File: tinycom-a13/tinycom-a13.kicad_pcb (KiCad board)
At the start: 4 copper layers, 39.4 x 41.1 mm, 23 parts, among them P1 CONN_02X08, P2 CONN_02X08, U1 IC_A13, U2 H5TQ2G83BFR/FBGA82, Y1 Crystal

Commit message: prepare base
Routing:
- net VCC_30: track 42.4 -> 45.3 mm
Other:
- rule pad_to_mask_clearance: 0.2 -> 0.07

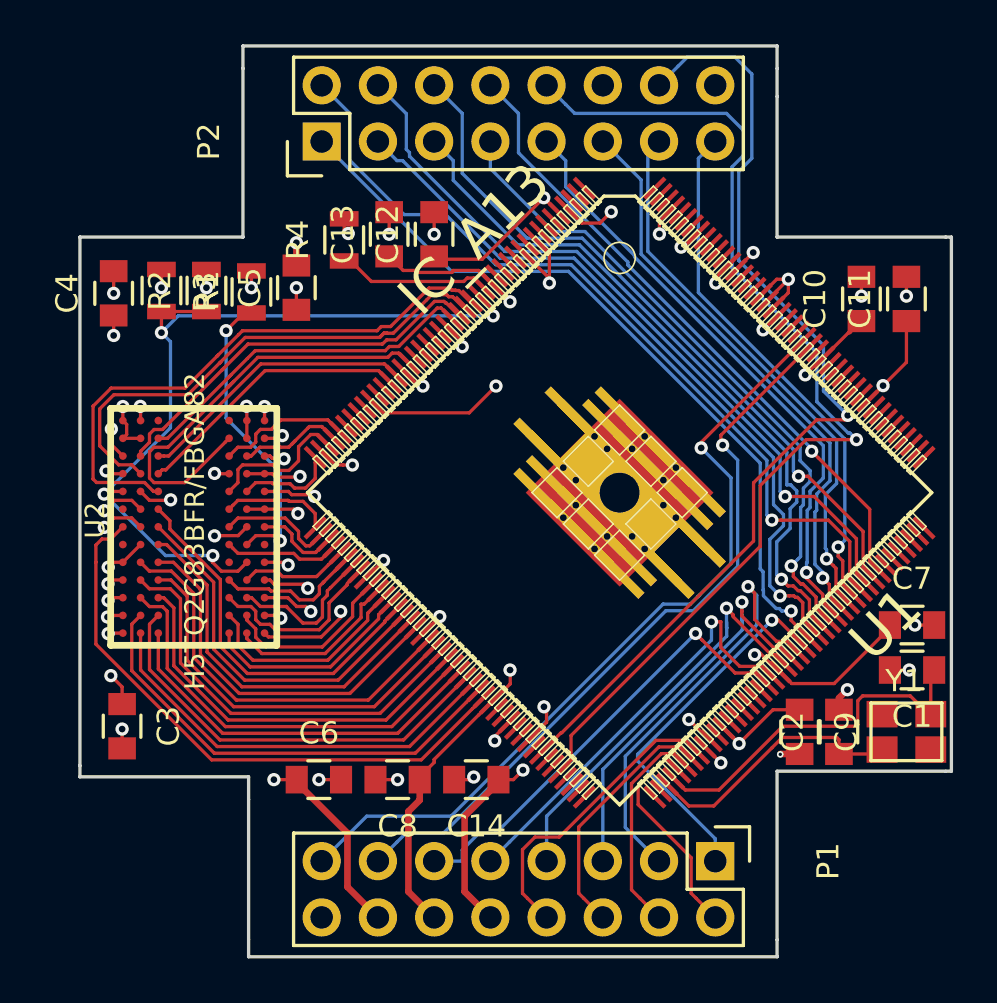
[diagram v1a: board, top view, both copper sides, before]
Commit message: change connectors
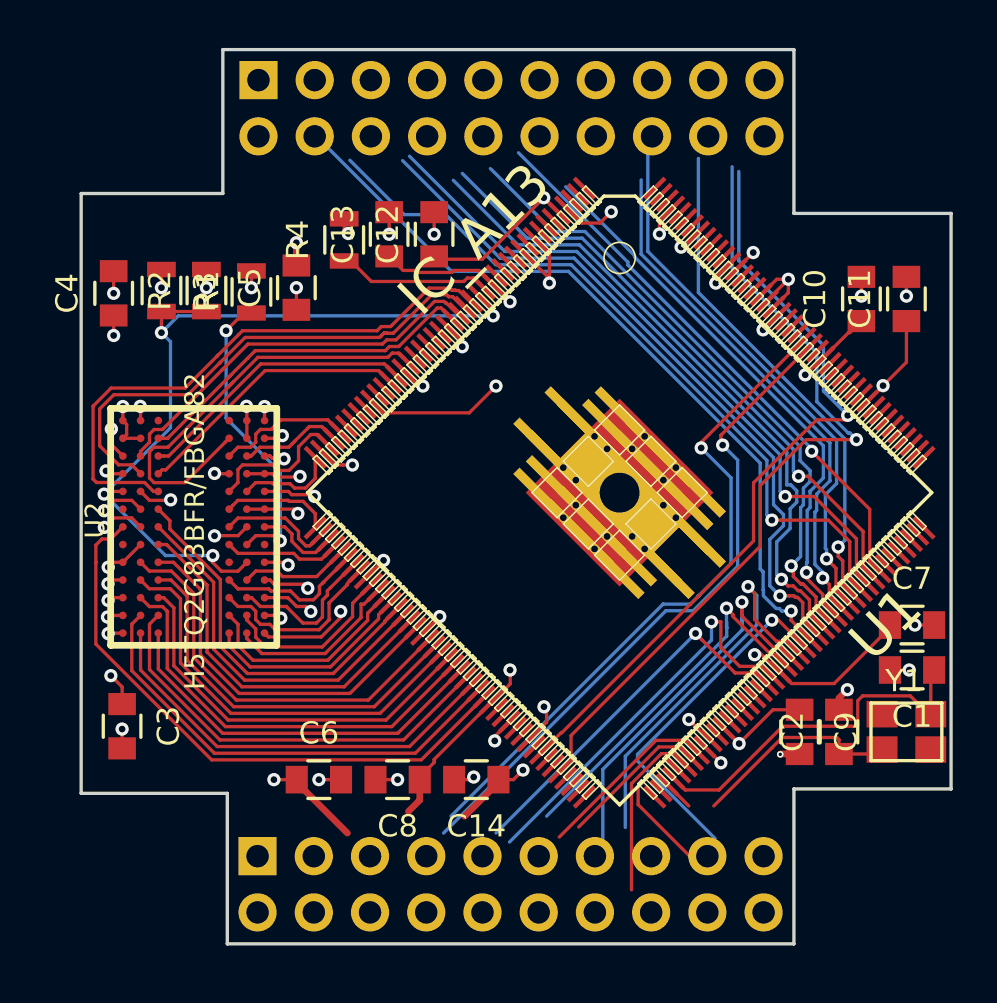
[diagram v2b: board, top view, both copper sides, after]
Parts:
- P1, P2: value CONN_02X08 -> CONN_02X10; footprint Pin_Headers:Pin_Header_Straight_2x08 -> Pin_Headers:Pin_Header_Straight_2x10; moved to B.Cu
- moved P1 20.7 mm to (93.4, 156.2)
- moved P2 3.98 mm to (93.4, 121.2), turned to 270 degrees
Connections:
- P1 pad 1: SDC0_D2 -> (no net)
- P1 pad 10: VCC_33 -> (no net)
- P1 pad 11: SDC0_D1 -> (no net)
- P1 pad 12: VCC_14 -> (no net)
- P1 pad 13: UART1_RX -> (no net)
- P1 pad 14: VCC_15 -> (no net)
- P1 pad 15: UART1_TX -> (no net)
- P1 pad 16: GND -> (no net)
- P1 pad 2: UDM0 -> (no net)
- P1 pad 3: SDC0_D3 -> (no net)
- P1 pad 4: UDP0 -> (no net)
- P1 pad 5: SDC0_CMD -> (no net)
- P1 pad 6: UDM1 -> (no net)
- P1 pad 7: SDC0_CLK -> (no net)
- P1 pad 8: UDP1 -> (no net)
- P1 pad 9: SDC0_D0 -> (no net)
- P2 pad 1: CSI_CLK -> (no net)
- P2 pad 10: MICIN1 -> (no net)
- P2 pad 11: CSI_D1 -> (no net)
- P2 pad 12: GND -> (no net)
- P2 pad 13: CSI_D2 -> (no net)
- P2 pad 14: VCC_30 -> (no net)
- P2 pad 15: CSI_D3 -> (no net)
- P2 pad 16: GND -> (no net)
- P2 pad 2: CSI_D4 -> (no net)
- P2 pad 3: CSI_MCLK -> (no net)
- P2 pad 4: CSI_D5 -> (no net)
- P2 pad 5: CSI_HSYNC -> (no net)
- P2 pad 6: CSI_D6 -> (no net)
- P2 pad 7: CSI_VSYNC -> (no net)
- P2 pad 8: CSI_D7 -> (no net)
- P2 pad 9: CSI_D0 -> (no net)
- U1 pad 1: Net-(U1-Pad1) -> (no net)
- U1 pad 10: Net-(U1-Pad10) -> (no net)
- U1 pad 101: Net-(U1-Pad101) -> (no net)
- U1 pad 102: Net-(U1-Pad102) -> (no net)
- U1 pad 103: Net-(U1-Pad103) -> (no net)
- U1 pad 104: Net-(U1-Pad104) -> (no net)
- U1 pad 105: Net-(U1-Pad105) -> (no net)
- U1 pad 106: Net-(U1-Pad106) -> (no net)
- U1 pad 107: SDC0_D1 -> (no net)
- U1 pad 108: SDC0_D0 -> (no net)
- U1 pad 110: SDC0_CLK -> (no net)
- U1 pad 111: SDC0_CMD -> (no net)
- U1 pad 112: SDC0_D3 -> (no net)
- U1 pad 113: SDC0_D2 -> (no net)
- U1 pad 114: CSI_CLK -> (no net)
- U1 pad 115: CSI_MCLK -> (no net)
- U1 pad 116: CSI_HSYNC -> (no net)
- U1 pad 117: CSI_VSYNC -> (no net)
- U1 pad 118: CSI_D0 -> (no net)
- U1 pad 119: CSI_D1 -> (no net)
- U1 pad 12: Net-(U1-Pad12) -> (no net)
- U1 pad 120: CSI_D2 -> (no net)
- U1 pad 121: CSI_D3 -> (no net)
- U1 pad 122: CSI_D4 -> (no net)
- U1 pad 123: CSI_D5 -> (no net)
- U1 pad 124: CSI_D6 -> (no net)
- U1 pad 125: CSI_D7 -> (no net)
- U1 pad 126: Net-(U1-Pad126) -> (no net)
- U1 pad 127: Net-(U1-Pad127) -> (no net)
- U1 pad 128: Net-(U1-Pad128) -> (no net)
- U1 pad 129: Net-(U1-Pad129) -> (no net)
- U1 pad 13: Net-(U1-Pad13) -> (no net)
- U1 pad 130: Net-(U1-Pad130) -> (no net)
- U1 pad 131: Net-(U1-Pad131) -> (no net)
- U1 pad 132: Net-(U1-Pad132) -> (no net)
- U1 pad 133: Net-(U1-Pad133) -> (no net)
- U1 pad 134: Net-(U1-Pad134) -> (no net)
- U1 pad 135: Net-(U1-Pad135) -> (no net)
- U1 pad 136: Net-(U1-Pad136) -> (no net)
- U1 pad 137: Net-(U1-Pad137) -> (no net)
- U1 pad 138: Net-(U1-Pad138) -> (no net)
- U1 pad 139: Net-(U1-Pad139) -> (no net)
- U1 pad 14: Net-(U1-Pad14) -> (no net)
- U1 pad 140: Net-(U1-Pad140) -> (no net)
- U1 pad 141: Net-(U1-Pad141) -> (no net)
- U1 pad 143: Net-(U1-Pad143) -> (no net)
- U1 pad 144: Net-(U1-Pad144) -> (no net)
- U1 pad 145: Net-(U1-Pad145) -> (no net)
- U1 pad 146: Net-(U1-Pad146) -> (no net)
- U1 pad 147: Net-(U1-Pad147) -> (no net)
- U1 pad 148: Net-(U1-Pad148) -> (no net)
- U1 pad 15: Net-(U1-Pad15) -> (no net)
- U1 pad 150: Net-(U1-Pad150) -> (no net)
- U1 pad 151: UART1_RX -> (no net)
- U1 pad 152: UART1_TX -> (no net)
- U1 pad 153: Net-(U1-Pad153) -> (no net)
- U1 pad 154: Net-(U1-Pad154) -> (no net)
- U1 pad 155: Net-(U1-Pad155) -> (no net)
- U1 pad 160: Net-(U1-Pad160) -> (no net)
- U1 pad 161: Net-(U1-Pad161) -> (no net)
- U1 pad 162: Net-(U1-Pad162) -> (no net)
- U1 pad 165: Net-(U1-Pad165) -> (no net)
- U1 pad 166: Net-(U1-Pad166) -> (no net)
- U1 pad 167: Net-(U1-Pad167) -> (no net)
- U1 pad 168: Net-(U1-Pad168) -> (no net)
- U1 pad 170: Net-(U1-Pad170) -> (no net)
- U1 pad 171: Net-(U1-Pad171) -> (no net)
- U1 pad 172: Net-(U1-Pad172) -> (no net)
- U1 pad 174: Net-(U1-Pad174) -> (no net)
- U1 pad 175: Net-(U1-Pad175) -> (no net)
- U1 pad 176: Net-(U1-Pad176) -> (no net)
- U1 pad 2: Net-(U1-Pad2) -> (no net)
- U1 pad 24: DDR3_D11 -> (no net)
- U1 pad 25: DDR3_D9 -> (no net)
- U1 pad 26: DDR3_D13 -> (no net)
- U1 pad 27: DDR3_D15 -> (no net)
- U1 pad 28: DDR3_DM1 -> (no net)
- U1 pad 3: Net-(U1-Pad3) -> (no net)
- U1 pad 33: DDR3_DQS1_P -> (no net)
- U1 pad 34: DDR3_DQS1_N -> (no net)
- U1 pad 36: DDR3_D12 -> (no net)
- U1 pad 37: DDR3_D8 -> (no net)
- U1 pad 38: DDR3_D14 -> (no net)
- U1 pad 39: DDR3_D10 -> (no net)
- U1 pad 6: Net-(U1-Pad6) -> (no net)
- U1 pad 7: Net-(U1-Pad7) -> (no net)
- U1 pad 74: Net-(U1-Pad74) -> (no net)
- U1 pad 75: Net-(U1-Pad75) -> (no net)
- U1 pad 77: Net-(U1-Pad77) -> (no net)
- U1 pad 78: Net-(U1-Pad78) -> (no net)
- U1 pad 8: Net-(U1-Pad8) -> (no net)
- U1 pad 80: Net-(U1-Pad80) -> (no net)
- U1 pad 81: VCC_30 -> (no net)
- U1 pad 82: Net-(U1-Pad82) -> (no net)
- U1 pad 83: Net-(U1-Pad83) -> (no net)
- U1 pad 84: MICIN1 -> (no net)
- U1 pad 85: Net-(U1-Pad85) -> (no net)
- U1 pad 86: Net-(U1-Pad86) -> (no net)
- U1 pad 87: Net-(U1-Pad87) -> (no net)
- U1 pad 88: Net-(U1-Pad88) -> (no net)
- U1 pad 89: Net-(U1-Pad89) -> (no net)
- U1 pad 90: Net-(U1-Pad90) -> (no net)
- U1 pad 93: UDM0 -> (no net)
- U1 pad 94: UDP0 -> (no net)
- U1 pad 95: UDM1 -> (no net)
- U1 pad 96: UDP1 -> (no net)
- U1 pad 99: Net-(U1-Pad99) -> (no net)
- U2 pad A3: Net-(U2-PadA3) -> (no net)
- U2 pad A7: Net-(U2-PadA7) -> (no net)
- U2 pad F1: Net-(U2-PadF1) -> (no net)
- U2 pad H1: Net-(U2-PadH1) -> (no net)
- U2 pad H9: Net-(U2-PadH9) -> (no net)
- U2 pad J7: Net-(U2-PadJ7) -> (no net)
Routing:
- net (no net): track 8.18 -> 614.6 mm, vias 0 -> 22
- net MICIN1: track 48.5 -> 0.00 mm, vias 1 -> 0
- net VCC_30: track 45.3 -> 0.00 mm, vias 1 -> 0
- net CSI_D4: track 37.5 -> 0.00 mm, vias 1 -> 0
- net UART1_TX: track 36.8 -> 0.00 mm, vias 1 -> 0
- net CSI_CLK: track 35.1 -> 0.00 mm, vias 1 -> 0
- net CSI_D5: track 34.4 -> 0.00 mm, vias 1 -> 0
- net UART1_RX: track 33.8 -> 0.00 mm, vias 1 -> 0
- net CSI_MCLK: track 33.5 -> 0.00 mm, vias 1 -> 0
- net CSI_D6: track 32.2 -> 0.00 mm, vias 1 -> 0
- net CSI_HSYNC: track 32.0 -> 0.00 mm, vias 1 -> 0
- net CSI_VSYNC: track 29.7 -> 0.00 mm, vias 1 -> 0
- net CSI_D7: track 29.3 -> 0.00 mm, vias 1 -> 0
- net CSI_D0: track 27.5 -> 0.00 mm, vias 1 -> 0
- net CSI_D1: track 26.2 -> 0.00 mm, vias 1 -> 0
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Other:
- board size 39.4 x 41.1 mm -> 39.3 x 40.4 mm
